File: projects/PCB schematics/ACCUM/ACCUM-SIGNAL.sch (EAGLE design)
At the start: 23 parts, among them J1 2P(90DEG)_1-770966-0, J2 2P(90DEG)_1-770966-0, J3 2P(90DEG)_1-770966-0, J4 2P(90DEG)_1-770966-0, J5 2P(90DEG)_1-770966-0, Q1 IRFZ44Z

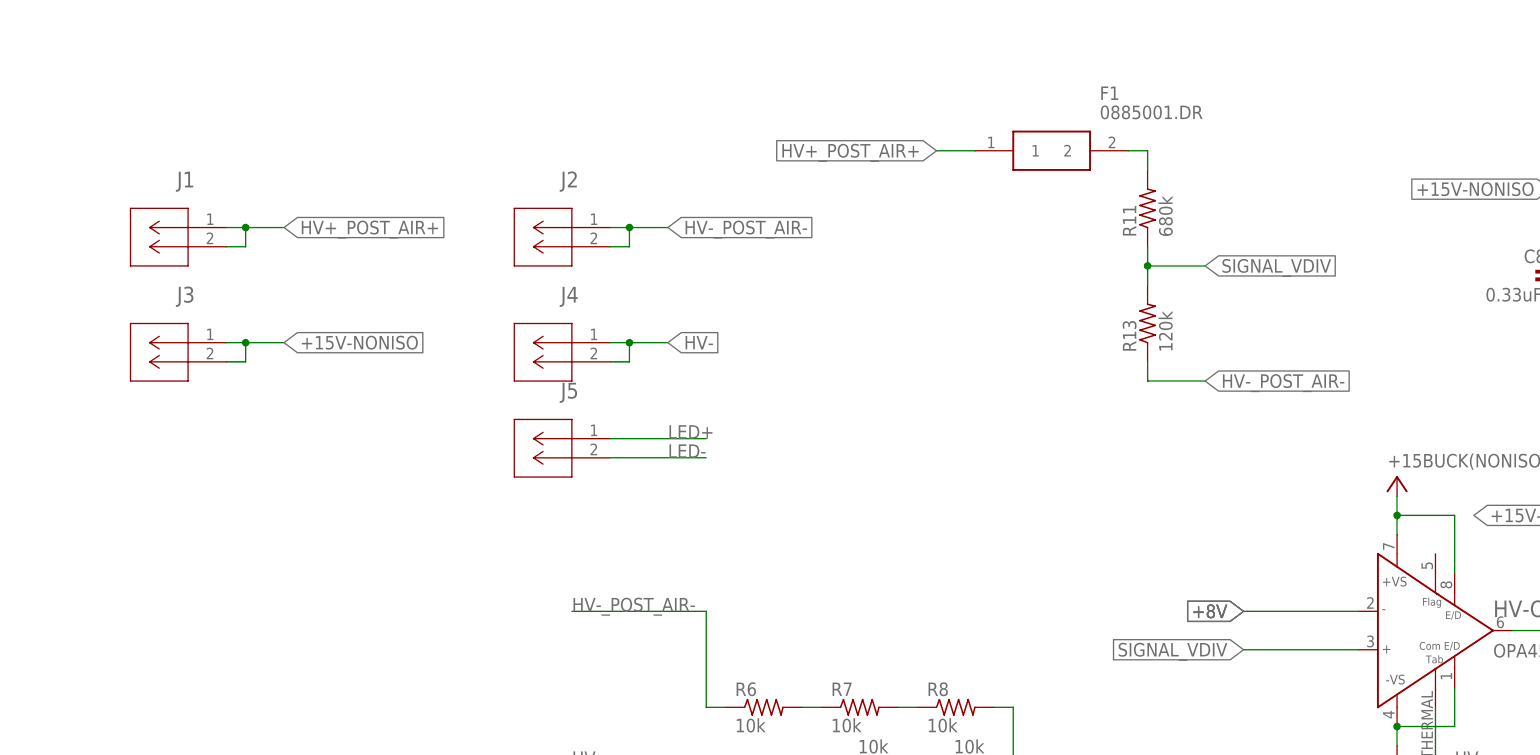
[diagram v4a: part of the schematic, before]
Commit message: PROJ - Silkscreen modifications - 50%.
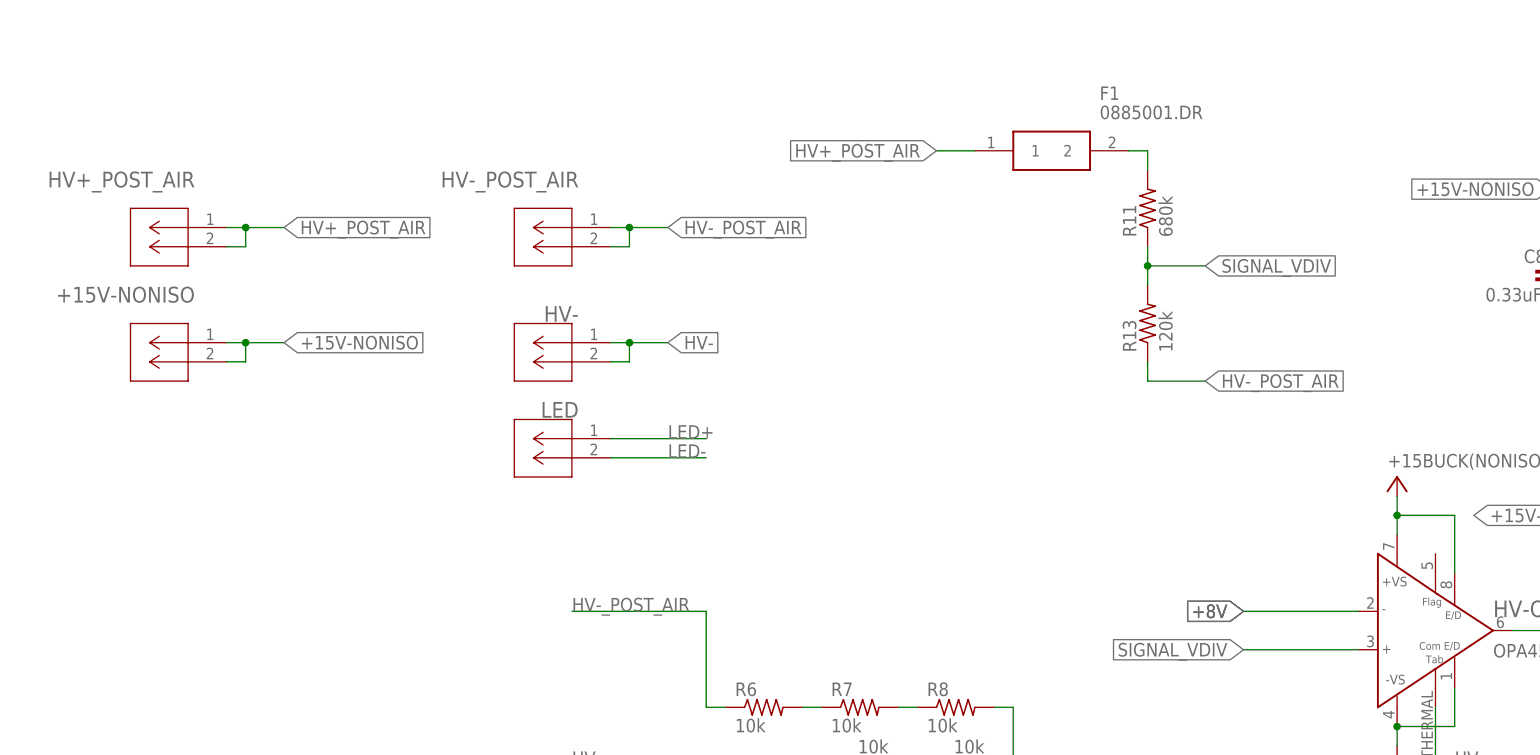
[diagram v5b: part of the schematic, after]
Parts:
- renumbered J1 to HV+_POST_AIR, J2 to HV-_POST_AIR, J3 to +15V-NONISO, J4 to HV-, J5 to LED
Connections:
- net HV+_POST_AIR+ renamed HV+_POST_AIR
- net HV-_POST_AIR- renamed HV-_POST_AIR
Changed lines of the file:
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@@
 <part name="SUPPLY15" library="supply2" library_urn="urn:adsk.eagle:library:372" deviceset="GND" device="" value="HV-"/>
 <part name="C10" library="rcl" library_urn="urn:adsk.eagle:library:334" deviceset="C-EU" device="C0805" package3d_urn="urn:adsk.eagle:package:23617/2" value="0.1uF"/>
-<part name="J1" library="con-MATE-N-LOK" deviceset="2P(90DEG)_1-770966-0" device=""/>
-<part name="J2" library="con-MATE-N-LOK" deviceset="2P(90DEG)_1-770966-0" device=""/>
-<part name="J4" library="con-MATE-N-LOK" deviceset="2P(90DEG)_1-770966-0" device=""/>
-<part name="J3" library="con-MATE-N-LOK" deviceset="2P(90DEG)_1-770966-0" device=""/>
-<part name="J5" library="con-MATE-N-LOK" deviceset="2P(90DEG)_1-770966-0" device=""/>
+<part name="HV+_POST_AIR" library="con-MATE-N-LOK" deviceset="2P(90DEG)_1-770966-0" device=""/>
+<part name="HV-_POST_AIR" library="con-MATE-N-LOK" deviceset="2P(90DEG)_1-770966-0" device=""/>
+<part name="HV-" library="con-MATE-N-LOK" deviceset="2P(90DEG)_1-770966-0" device=""/>
+<part name="+15V-NONISO" library="con-MATE-N-LOK" deviceset="2P(90DEG)_1-770966-0" device=""/>
+<part name="LED" library="con-MATE-N-LOK" deviceset="2P(90DEG)_1-770966-0" device=""/>
 <part name="R1" library="rcl" library_urn="urn:adsk.eagle:library:334" deviceset="R-US_" device="R0805" package3d_urn="urn:adsk.eagle:package:23553/2" value="100k"/>
 <part name="R2" library="rcl" library_urn="urn:adsk.eagle:library:334" deviceset="R-US_" device="R0805" package3d_urn="urn:adsk.eagle:package:23553/2" value="100"/>
@@
 <attribute name="VALUE" x="235.204" y="81.661" size="1.778" layer="96"/>
 </instance>
-<instance part="J1" gate="A" x="25.4" y="91.44" smashed="yes" rot="MR0">
+<instance part="HV+_POST_AIR" gate="A" x="25.4" y="91.44" smashed="yes" rot="MR0">
 <attribute name="NAME" x="21.2344" y="96.7486" size="2.0828" layer="95" ratio="6" rot="SMR0"/>
 </instance>
-<instance part="J2" gate="A" x="76.2" y="91.44" smashed="yes" rot="MR0">
+<instance part="HV-_POST_AIR" gate="A" x="76.2" y="91.44" smashed="yes" rot="MR0">
 <attribute name="NAME" x="72.0344" y="96.7486" size="2.0828" layer="95" ratio="6" rot="SMR0"/>
 </instance>
-<instance part="J4" gate="A" x="76.2" y="76.2" smashed="yes" rot="MR0">
-<attribute name="NAME" x="72.0344" y="81.5086" size="2.0828" layer="95" ratio="6" rot="SMR0"/>
-</instance>
-<instance part="J3" gate="A" x="25.4" y="76.2" smashed="yes" rot="MR0">
+<instance part="HV-" gate="A" x="76.2" y="76.2" smashed="yes" rot="MR0">
+<attribute name="NAME" x="72.0344" y="78.9686" size="2.0828" layer="95" ratio="6" rot="SMR0"/>
+</instance>
+<instance part="+15V-NONISO" gate="A" x="25.4" y="76.2" smashed="yes" rot="MR0">
 <attribute name="NAME" x="21.2344" y="81.5086" size="2.0828" layer="95" ratio="6" rot="SMR0"/>
 </instance>
-<instance part="J5" gate="A" x="76.2" y="63.5" smashed="yes" rot="MR0">
-<attribute name="NAME" x="72.0344" y="68.8086" size="2.0828" layer="95" ratio="6" rot="SMR0"/>
+<instance part="LED" gate="A" x="76.2" y="63.5" smashed="yes" rot="MR0">
+<attribute name="NAME" x="72.0344" y="66.2686" size="2.0828" layer="95" ratio="6" rot="SMR0"/>
 </instance>
 <instance part="R1" gate="G$1" x="213.36" y="30.48" smashed="yes" rot="R90">
@@
 <junction x="78.74" y="76.2"/>
 <label x="83.82" y="76.2" size="1.778" layer="95" xref="yes"/>
-<pinref part="J4" gate="A" pin="1"/>
-<pinref part="J4" gate="A" pin="2"/>
+<pinref part="HV-" gate="A" pin="1"/>
+<pinref part="HV-" gate="A" pin="2"/>
 </segment>
 <segment>
@@
 </segment>
 </net>
-<net name="HV+_POST_AIR+" class="0">
+<net name="HV+_POST_AIR" class="0">
 <segment>
 <wire x1="25.4" y1="91.44" x2="27.94" y2="91.44" width="0.1524" layer="91"/>
@@
 <junction x="27.94" y="91.44"/>
 <label x="33.02" y="91.44" size="1.778" layer="95" xref="yes"/>
-<pinref part="J1" gate="A" pin="1"/>
-<pinref part="J1" gate="A" pin="2"/>
+<pinref part="HV+_POST_AIR" gate="A" pin="1"/>
+<pinref part="HV+_POST_AIR" gate="A" pin="2"/>
 </segment>
 <segment>
@@
 <junction x="27.94" y="76.2"/>
 <label x="33.02" y="76.2" size="1.778" layer="95" xref="yes"/>
-<pinref part="J3" gate="A" pin="1"/>
-<pinref part="J3" gate="A" pin="2"/>
+<pinref part="+15V-NONISO" gate="A" pin="1"/>
+<pinref part="+15V-NONISO" gate="A" pin="2"/>
 </segment>
 <segment>
@@
 </segment>
 </net>
-<net name="HV-_POST_AIR-" class="0">
+<net name="HV-_POST_AIR" class="0">
 <segment>
 <wire x1="76.2" y1="91.44" x2="78.74" y2="91.44" width="0.1524" layer="91"/>
@@
 <junction x="78.74" y="91.44"/>
 <label x="83.82" y="91.44" size="1.778" layer="95" xref="yes"/>
-<pinref part="J2" gate="A" pin="1"/>
-<pinref part="J2" gate="A" pin="2"/>
+<pinref part="HV-_POST_AIR" gate="A" pin="1"/>
+<pinref part="HV-_POST_AIR" gate="A" pin="2"/>
 </segment>
 <segment>
@@
 <net name="LED+" class="0">
 <segment>
-<pinref part="J5" gate="A" pin="1"/>
+<pinref part="LED" gate="A" pin="1"/>
 <wire x1="76.2" y1="63.5" x2="88.9" y2="63.5" width="0.1524" layer="91"/>
 <label x="83.82" y="63.5" size="1.778" layer="95"/>
@@
 <net name="LED-" class="0">
 <segment>
-<pinref part="J5" gate="A" pin="2"/>
+<pinref part="LED" gate="A" pin="2"/>
 <wire x1="76.2" y1="60.96" x2="88.9" y2="60.96" width="0.1524" layer="91"/>
 <label x="83.82" y="60.96" size="1.778" layer="95"/>

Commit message: PROJ - Gerber files major milestone - 05/05/19.
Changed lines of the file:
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@@
 <label x="236.22" y="76.2" size="1.778" layer="95" xref="yes"/>
 <wire x1="233.68" y1="76.2" x2="236.22" y2="76.2" width="0.1524" layer="91"/>
+<junction x="233.68" y="76.2"/>
 </segment>
 <segment>
@@
 </sheet>
 </sheets>
+<errors>
+</errors>
 </schematic>
 </drawing>
